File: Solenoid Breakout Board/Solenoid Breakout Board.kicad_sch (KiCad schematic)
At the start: 69 parts, among them J1 Solenoid In, J2 Pwr IN, J3 Pwr OUT, Q1 IRF540N, Q2 IRF540N, Q3 IRF540N, Q4 IRF540N, Q5 IRF540N, Q6 IRF540N, Q7 IRF540N, Q8 IRF540N, Q9 IRF540N, U1 LTV-247, U2 LTV-247, U3 LTV-247

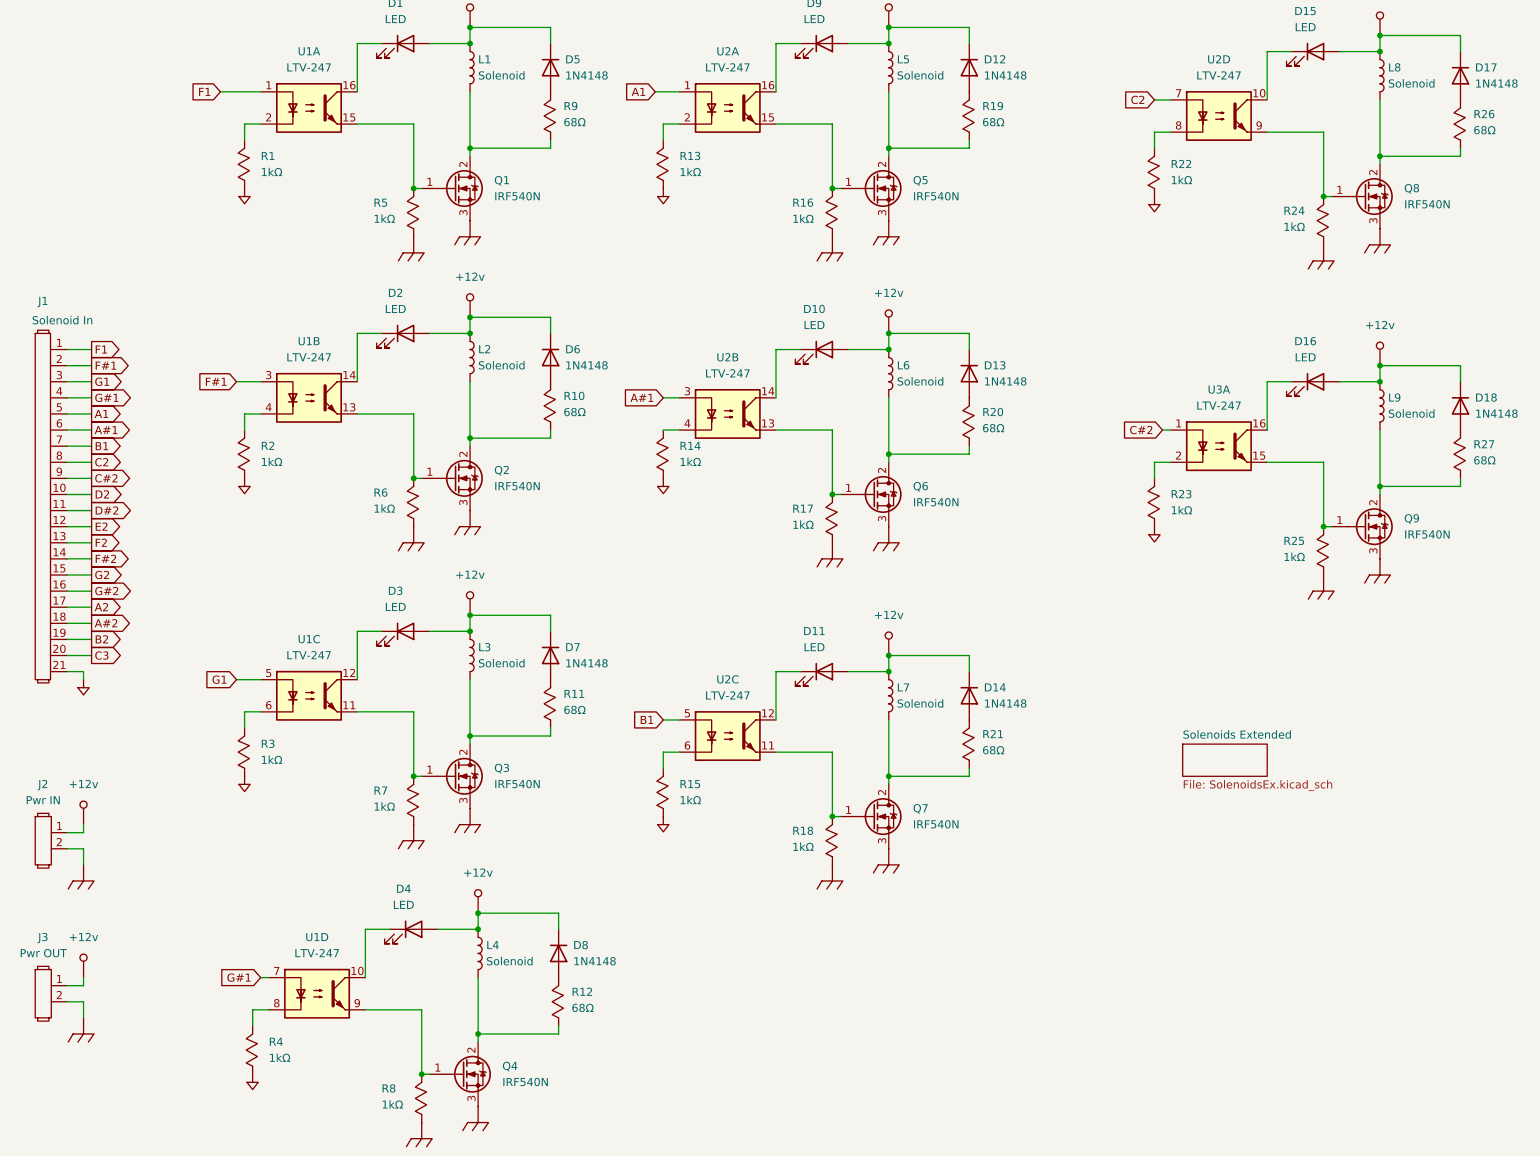
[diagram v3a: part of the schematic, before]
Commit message: replaced footprints on breakout to match new components
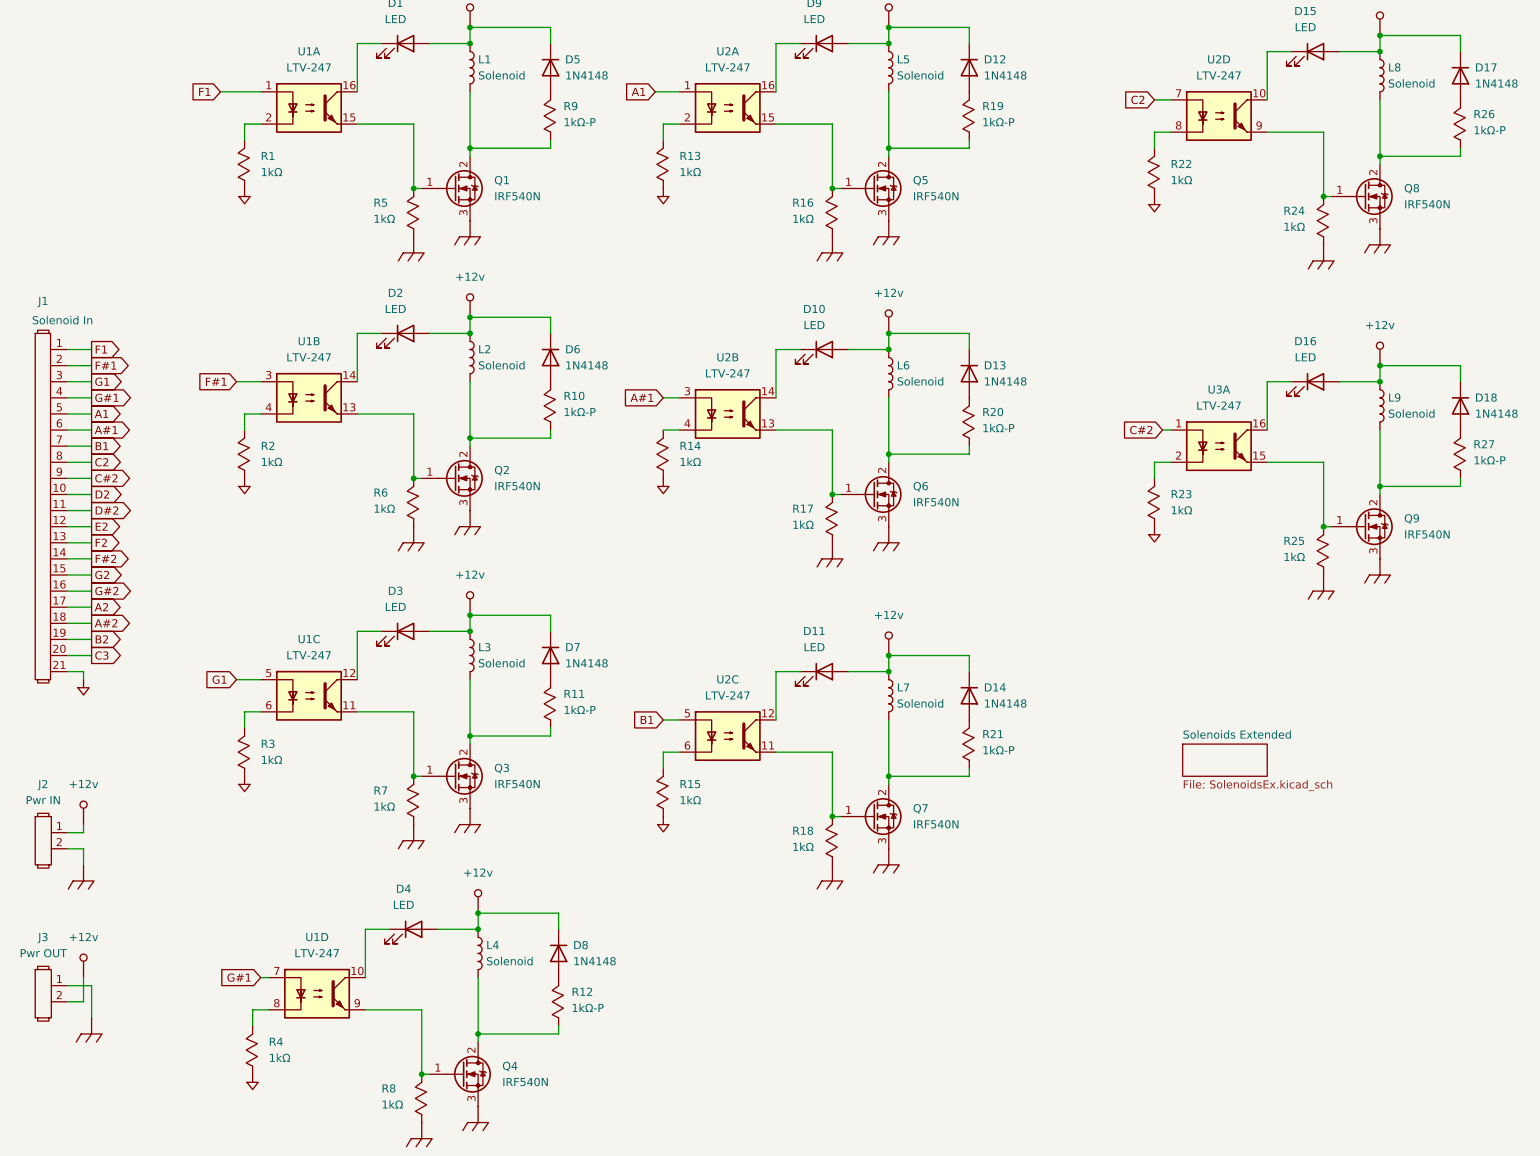
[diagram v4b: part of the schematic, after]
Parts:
- Q1, Q2, Q3, Q4, Q5, Q6, Q7, Q8, Q9: footprint Package_TO_SOT_THT:TO-220-3_Vertical -> Package_TO_SOT_THT:TO-220-3_Horizontal_TabUp
- R10, R11, R12, R19, R20, R21, R26, R27, R9: value 68Ω -> 1kΩ-P; footprint Resistor_SMD:R_0805_2012Metric_Pad1.20x1.40mm_HandSolder -> Resistor_SMD:R_1206_3216Metric_Pad1.30x1.75mm_HandSolder
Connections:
- net +12v: now also J3.2; no longer J3.1
- net Chassis_GND: now also J3.1; no longer J3.2
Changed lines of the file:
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@@
 	(wire
 		(pts
+			(xy 22.86 171.45) (xy 22.86 175.26)
+		)
+		(stroke
+			(width 0)
+			(type default)
+		)
+	)
+	(wire
+		(pts
 			(xy 194.31 38.1) (xy 191.77 38.1)
 		)
@@
 	(wire
 		(pts
-			(xy 22.86 175.26) (xy 22.86 177.8)
-		)
-		(stroke
-			(width 0)
-			(type default)
-		)
-	)
-	(wire
-		(pts
 			(xy 149.86 21.59) (xy 162.56 21.59)
 		)
@@
 	(wire
 		(pts
-			(xy 22.86 172.72) (xy 22.86 171.45)
-		)
-		(stroke
-			(width 0)
-			(type default)
-		)
-	)
-	(wire
-		(pts
 			(xy 116.84 36.83) (xy 114.3 36.83)
 		)
@@
 	(wire
 		(pts
-			(xy 20.32 172.72) (xy 22.86 172.72)
+			(xy 20.32 172.72) (xy 24.13 172.72)
 		)
 		(stroke
@@
 	(wire
 		(pts
+			(xy 24.13 172.72) (xy 24.13 177.8)
+		)
+		(stroke
+			(width 0)
+			(type default)
+		)
+	)
+	(wire
+		(pts
 			(xy 162.56 40.64) (xy 162.56 39.37)
 		)
@@
 			)
 		)
-		(property "Footprint" "Package_TO_SOT_THT:TO-220-3_Vertical"
+		(property "Footprint" "Package_TO_SOT_THT:TO-220-3_Horizontal_TabUp"
 			(at 86.36 48.895 0)
 			(effects
@@
 			)
 		)
-		(property "Footprint" "Package_TO_SOT_THT:TO-220-3_Vertical"
+		(property "Footprint" "Package_TO_SOT_THT:TO-220-3_Horizontal_TabUp"
 			(at 152.4 48.895 0)
 			(effects
@@
 			)
 		)
-		(property "Value" "68Ω"
+		(property "Value" "1kΩ-P"
 			(at 164.592 36.576 90)
 			(effects
@@
 			)
 		)
-		(property "Footprint" "Resistor_SMD:R_0805_2012Metric_Pad1.20x1.40mm_HandSolder"
+		(property "Footprint" "Resistor_SMD:R_1206_3216Metric_Pad1.30x1.75mm_HandSolder"
 			(at 160.02 36.83 0)
 			(effects
@@
 	(symbol
 		(lib_id "Custom Power:Chassis_GND")
-		(at 22.86 177.8 0)
+		(at 24.13 177.8 0)
 		(unit 1)
 		(exclude_from_sim no)
@@
 		(fields_autoplaced yes)
 		(property "Reference" "#PWR05"
-			(at 22.86 176.53 0)
+			(at 24.13 176.53 0)
 			(effects
 				(font
@@
 		)
 		(property "Value" "Chassis_GND"
-			(at 22.86 176.53 0)
+			(at 24.13 176.53 0)
 			(effects
 				(font
@@
 		)
 		(property "Footprint" ""
-			(at 22.86 176.53 0)
+			(at 24.13 176.53 0)
 			(effects
 				(font
@@
 		)
 		(property "Datasheet" ""
-			(at 22.86 176.53 0)
+			(at 24.13 176.53 0)
 			(effects
 				(font
@@
 		)
 		(property "Description" ""
-			(at 22.86 177.8 0)
+			(at 24.13 177.8 0)
 			(effects
 				(font
@@
 			)
 		)
-		(property "Footprint" "Package_TO_SOT_THT:TO-220-3_Vertical"
+		(property "Footprint" "Package_TO_SOT_THT:TO-220-3_Horizontal_TabUp"
 			(at 229.87 50.165 0)
 			(effects
@@
 			)
 		)
-		(property "Footprint" "Package_TO_SOT_THT:TO-220-3_Vertical"
+		(property "Footprint" "Package_TO_SOT_THT:TO-220-3_Horizontal_TabUp"
 			(at 229.87 102.235 0)
 			(effects
@@
 			)
 		)
-		(property "Value" "68Ω"
+		(property "Value" "1kΩ-P"
 			(at 242.062 89.916 90)
 			(effects
@@
 			)
 		)
-		(property "Footprint" "Resistor_SMD:R_0805_2012Metric_Pad1.20x1.40mm_HandSolder"
+		(property "Footprint" "Resistor_SMD:R_1206_3216Metric_Pad1.30x1.75mm_HandSolder"
 			(at 237.49 90.17 0)
 			(effects
@@
 			)
 		)
-		(property "Footprint" "Package_TO_SOT_THT:TO-220-3_Vertical"
+		(property "Footprint" "Package_TO_SOT_THT:TO-220-3_Horizontal_TabUp"
 			(at 86.36 94.615 0)
 			(effects
@@
 			)
 		)
-		(property "Footprint" "Package_TO_SOT_THT:TO-220-3_Vertical"
+		(property "Footprint" "Package_TO_SOT_THT:TO-220-3_Horizontal_TabUp"
 			(at 152.4 97.155 0)
 			(effects
@@
 			)
 		)
-		(property "Value" "68Ω"
+		(property "Value" "1kΩ-P"
 			(at 242.062 37.846 90)
 			(effects
@@
 			)
 		)
-		(property "Footprint" "Resistor_SMD:R_0805_2012Metric_Pad1.20x1.40mm_HandSolder"
+		(property "Footprint" "Resistor_SMD:R_1206_3216Metric_Pad1.30x1.75mm_HandSolder"
 			(at 237.49 38.1 0)
 			(effects
@@
 			)
 		)
-		(property "Value" "68Ω"
+		(property "Value" "1kΩ-P"
 			(at 98.552 129.286 90)
 			(effects
@@
 			)
 		)
-		(property "Footprint" "Resistor_SMD:R_0805_2012Metric_Pad1.20x1.40mm_HandSolder"
+		(property "Footprint" "Resistor_SMD:R_1206_3216Metric_Pad1.30x1.75mm_HandSolder"
 			(at 93.98 129.54 0)
 			(effects
@@
 			)
 		)
-		(property "Footprint" "Package_TO_SOT_THT:TO-220-3_Vertical"
+		(property "Footprint" "Package_TO_SOT_THT:TO-220-3_Horizontal_TabUp"
 			(at 87.63 188.595 0)
 			(effects
@@
 			)
 		)
-		(property "Value" "68Ω"
+		(property "Value" "1kΩ-P"
 			(at 164.592 84.836 90)
 			(effects
@@
 			)
 		)
-		(property "Footprint" "Resistor_SMD:R_0805_2012Metric_Pad1.20x1.40mm_HandSolder"
+		(property "Footprint" "Resistor_SMD:R_1206_3216Metric_Pad1.30x1.75mm_HandSolder"
 			(at 160.02 85.09 0)
 			(effects
@@
 			)
 		)
-		(property "Value" "68Ω"
+		(property "Value" "1kΩ-P"
 			(at 98.552 36.576 90)
 			(effects
@@
 			)
 		)
-		(property "Footprint" "Resistor_SMD:R_0805_2012Metric_Pad1.20x1.40mm_HandSolder"
+		(property "Footprint" "Resistor_SMD:R_1206_3216Metric_Pad1.30x1.75mm_HandSolder"
 			(at 93.98 36.83 0)
 			(effects
@@
 			)
 		)
-		(property "Value" "68Ω"
+		(property "Value" "1kΩ-P"
 			(at 99.822 176.276 90)
 			(effects
@@
 			)
 		)
-		(property "Footprint" "Resistor_SMD:R_0805_2012Metric_Pad1.20x1.40mm_HandSolder"
+		(property "Footprint" "Resistor_SMD:R_1206_3216Metric_Pad1.30x1.75mm_HandSolder"
 			(at 95.25 176.53 0)
 			(effects
@@
 			)
 		)
-		(property "Value" "68Ω"
+		(property "Value" "1kΩ-P"
 			(at 98.552 82.296 90)
 			(effects
@@
 			)
 		)
-		(property "Footprint" "Resistor_SMD:R_0805_2012Metric_Pad1.20x1.40mm_HandSolder"
+		(property "Footprint" "Resistor_SMD:R_1206_3216Metric_Pad1.30x1.75mm_HandSolder"
 			(at 93.98 82.55 0)
 			(effects
@@
 			)
 		)
-		(property "Footprint" "Package_TO_SOT_THT:TO-220-3_Vertical"
+		(property "Footprint" "Package_TO_SOT_THT:TO-220-3_Horizontal_TabUp"
 			(at 152.4 147.955 0)
 			(effects
@@
 			)
 		)
-		(property "Footprint" "Package_TO_SOT_THT:TO-220-3_Vertical"
+		(property "Footprint" "Package_TO_SOT_THT:TO-220-3_Horizontal_TabUp"
 			(at 86.36 141.605 0)
 			(effects
@@
 			)
 		)
-		(property "Value" "68Ω"
+		(property "Value" "1kΩ-P"
 			(at 164.592 135.636 90)
 			(effects
@@
 			)
 		)
-		(property "Footprint" "Resistor_SMD:R_0805_2012Metric_Pad1.20x1.40mm_HandSolder"
+		(property "Footprint" "Resistor_SMD:R_1206_3216Metric_Pad1.30x1.75mm_HandSolder"
 			(at 160.02 135.89 0)
 			(effects

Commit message: added pcb sheets
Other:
- note added: "For Plucking unit only solder components for L1-L12"
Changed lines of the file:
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@@
 		(rev "B")
 	)
+	(text "For Plucking unit only solder components for L1-L12"
+		(exclude_from_sim no)
+		(at 131.572 200.152 0)
+		(effects
+			(font
+				(size 1.27 1.27)
+			)
+		)
+	)
 	(junction
 		(at 85.09 180.34)
@@
 		)
 		(fill
-			(color 0 0 0 0.0000)
+			(color 255 255 194 1.0000)
 		)
 		(property "Sheetname" "Solenoids Extended"
